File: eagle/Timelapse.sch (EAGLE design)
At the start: 11 parts, among them U1 ATTINY2313V-10PU, X1 1501_04

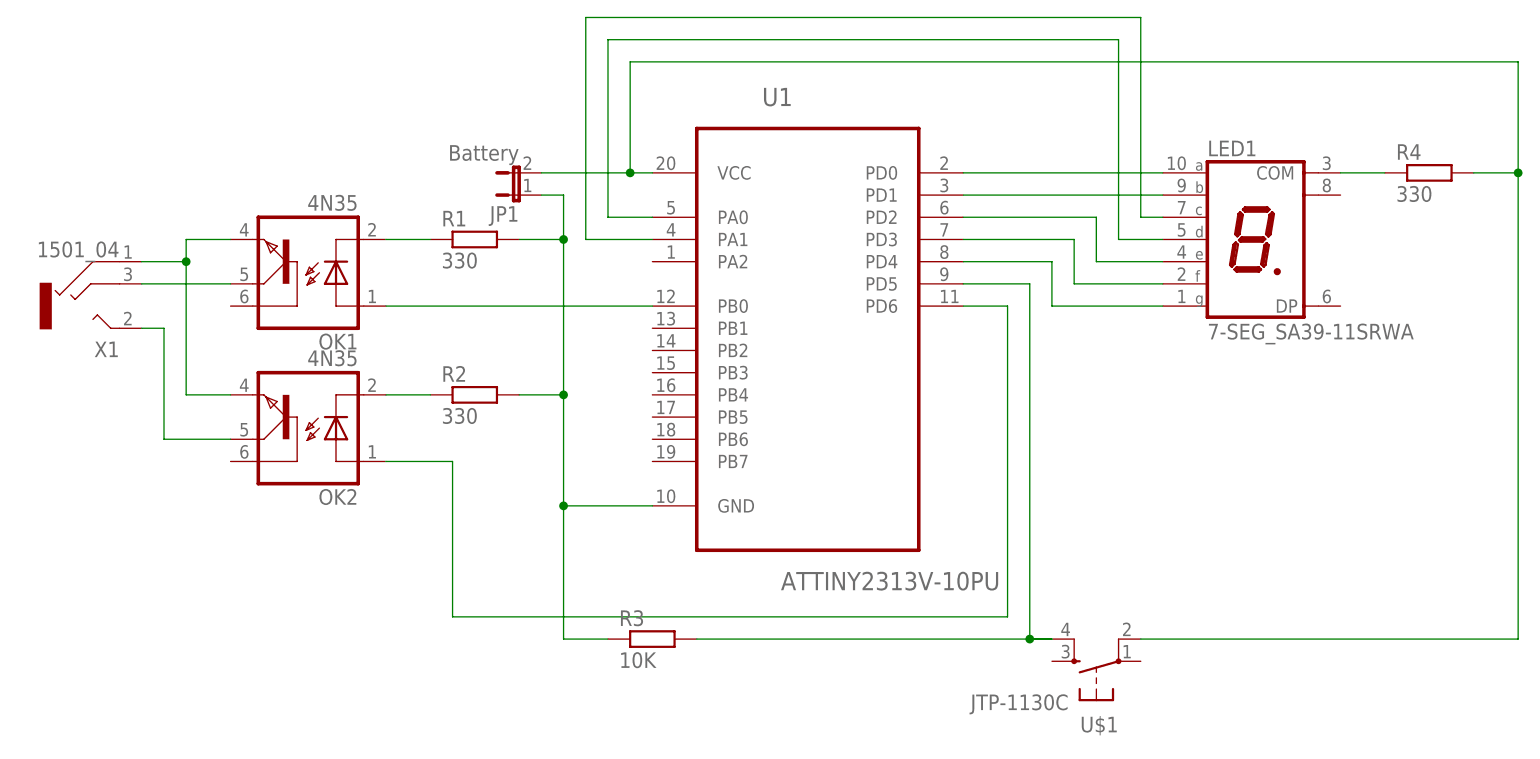
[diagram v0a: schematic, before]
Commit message: updated eagle with small changes
-move jumper
-rearrange diagram
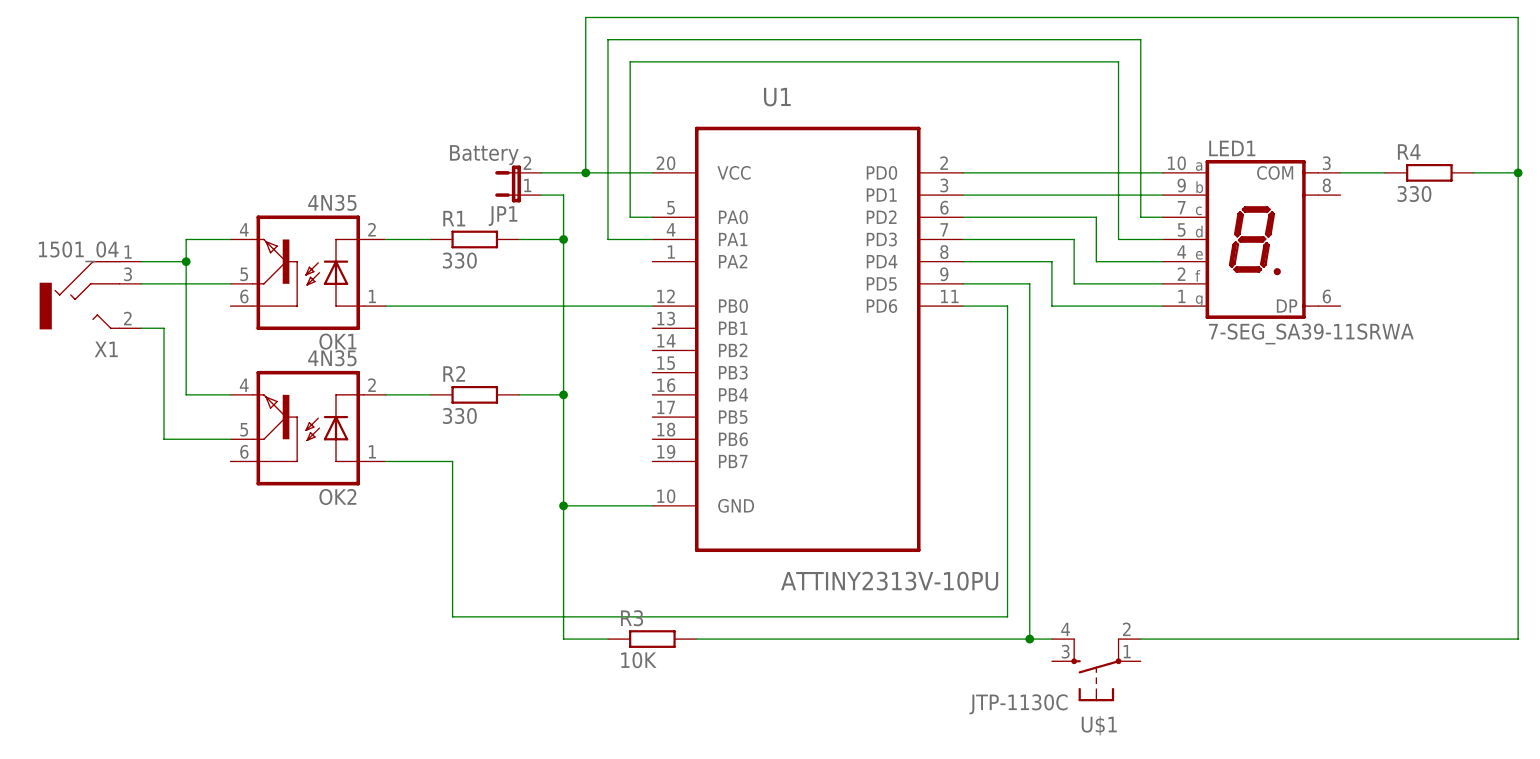
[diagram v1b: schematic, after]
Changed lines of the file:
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@@
 <segment>
 <pinref part="U1" gate="A" pin="PA1"/>
-<wire x1="40.64" y1="68.58" x2="33.02" y2="68.58" width="0.1524" layer="91"/>
-<wire x1="33.02" y1="68.58" x2="33.02" y2="93.98" width="0.1524" layer="91"/>
-<wire x1="33.02" y1="93.98" x2="96.52" y2="93.98" width="0.1524" layer="91"/>
-<wire x1="96.52" y1="93.98" x2="96.52" y2="71.12" width="0.1524" layer="91"/>
+<wire x1="40.64" y1="68.58" x2="35.56" y2="68.58" width="0.1524" layer="91"/>
+<wire x1="35.56" y1="68.58" x2="35.56" y2="91.44" width="0.1524" layer="91"/>
+<wire x1="35.56" y1="91.44" x2="96.52" y2="91.44" width="0.1524" layer="91"/>
+<wire x1="96.52" y1="91.44" x2="96.52" y2="71.12" width="0.1524" layer="91"/>
 <wire x1="96.52" y1="71.12" x2="99.06" y2="71.12" width="0.1524" layer="91"/>
 <pinref part="LED1" gate="G$1" pin="C"/>
@@
 <net name="N$7" class="0">
 <segment>
-<wire x1="40.64" y1="71.12" x2="35.56" y2="71.12" width="0.1524" layer="91"/>
-<wire x1="35.56" y1="71.12" x2="35.56" y2="91.44" width="0.1524" layer="91"/>
-<wire x1="35.56" y1="91.44" x2="93.98" y2="91.44" width="0.1524" layer="91"/>
-<wire x1="93.98" y1="91.44" x2="93.98" y2="68.58" width="0.1524" layer="91"/>
+<wire x1="40.64" y1="71.12" x2="38.1" y2="71.12" width="0.1524" layer="91"/>
+<wire x1="38.1" y1="71.12" x2="38.1" y2="88.9" width="0.1524" layer="91"/>
+<wire x1="38.1" y1="88.9" x2="93.98" y2="88.9" width="0.1524" layer="91"/>
+<wire x1="93.98" y1="88.9" x2="93.98" y2="68.58" width="0.1524" layer="91"/>
 <wire x1="93.98" y1="68.58" x2="99.06" y2="68.58" width="0.1524" layer="91"/>
 <pinref part="LED1" gate="G$1" pin="D"/>
@@
 <segment>
 <pinref part="U1" gate="A" pin="VCC"/>
-<wire x1="40.64" y1="76.2" x2="38.1" y2="76.2" width="0.1524" layer="91"/>
-<wire x1="38.1" y1="76.2" x2="38.1" y2="88.9" width="0.1524" layer="91"/>
-<wire x1="38.1" y1="88.9" x2="139.7" y2="88.9" width="0.1524" layer="91"/>
-<wire x1="139.7" y1="88.9" x2="139.7" y2="76.2" width="0.1524" layer="91"/>
+<wire x1="40.64" y1="76.2" x2="33.02" y2="76.2" width="0.1524" layer="91"/>
+<wire x1="33.02" y1="76.2" x2="33.02" y2="93.98" width="0.1524" layer="91"/>
+<wire x1="33.02" y1="93.98" x2="139.7" y2="93.98" width="0.1524" layer="91"/>
+<wire x1="139.7" y1="93.98" x2="139.7" y2="76.2" width="0.1524" layer="91"/>
 <pinref part="R4" gate="G$1" pin="2"/>
 <wire x1="139.7" y1="76.2" x2="134.62" y2="76.2" width="0.1524" layer="91"/>
 <junction x="139.7" y="76.2"/>
 <wire x1="139.7" y1="22.86" x2="139.7" y2="76.2" width="0.1524" layer="91"/>
-<wire x1="38.1" y1="76.2" x2="27.94" y2="76.2" width="0.1524" layer="91"/>
+<wire x1="33.02" y1="76.2" x2="27.94" y2="76.2" width="0.1524" layer="91"/>
 <pinref part="JP1" gate="A" pin="2"/>
-<junction x="38.1" y="76.2"/>
+<junction x="33.02" y="76.2"/>
 <pinref part="U$1" gate="S$1" pin="P1"/>
 <wire x1="96.52" y1="22.86" x2="139.7" y2="22.86" width="0.1524" layer="91"/>
@@
 <wire x1="76.2" y1="63.5" x2="83.82" y2="63.5" width="0.1524" layer="91"/>
 <wire x1="83.82" y1="63.5" x2="83.82" y2="22.86" width="0.1524" layer="91"/>
-<wire x1="83.82" y1="22.86" x2="86.36" y2="22.86" width="0.1524" layer="91"/>
 <wire x1="86.36" y1="22.86" x2="83.82" y2="22.86" width="0.1524" layer="91"/>
 <pinref part="R3" gate="G$1" pin="2"/>
